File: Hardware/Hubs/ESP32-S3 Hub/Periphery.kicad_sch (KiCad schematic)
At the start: 13 parts, among them SW1 Mitsumi R-667996, SW2 Mitsumi R-667996, SW3 DS04-254-2-04BK-SMT, U2 74HC595, U3 THVD1420DRLR

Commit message: Started Proto 2 again
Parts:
- removed R21, R22, R23: 120 ohm, Resistor_SMD:R_0402_1005Metric, symbol Device:R_Small
- removed SW3: DS04-254-2-04BK-SMT, Button_Switch_SMD:SW_DIP_SPSTx04_Slide_Omron_A6S-410x_W8.9mm_P2.54mm, symbol Switch:SW_DIP_x04
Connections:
- no-connect marks 4 -> 2

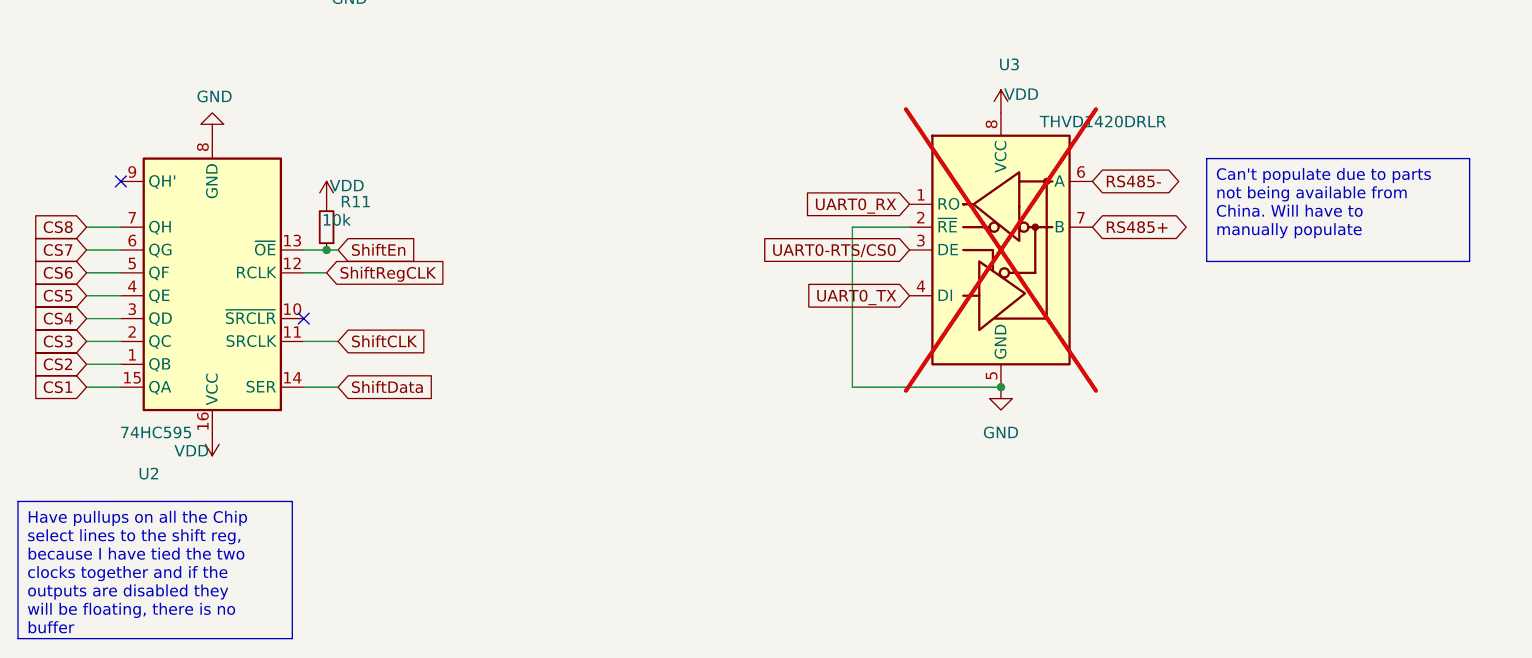
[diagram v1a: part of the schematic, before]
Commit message: Updated connectors in schem and pcb
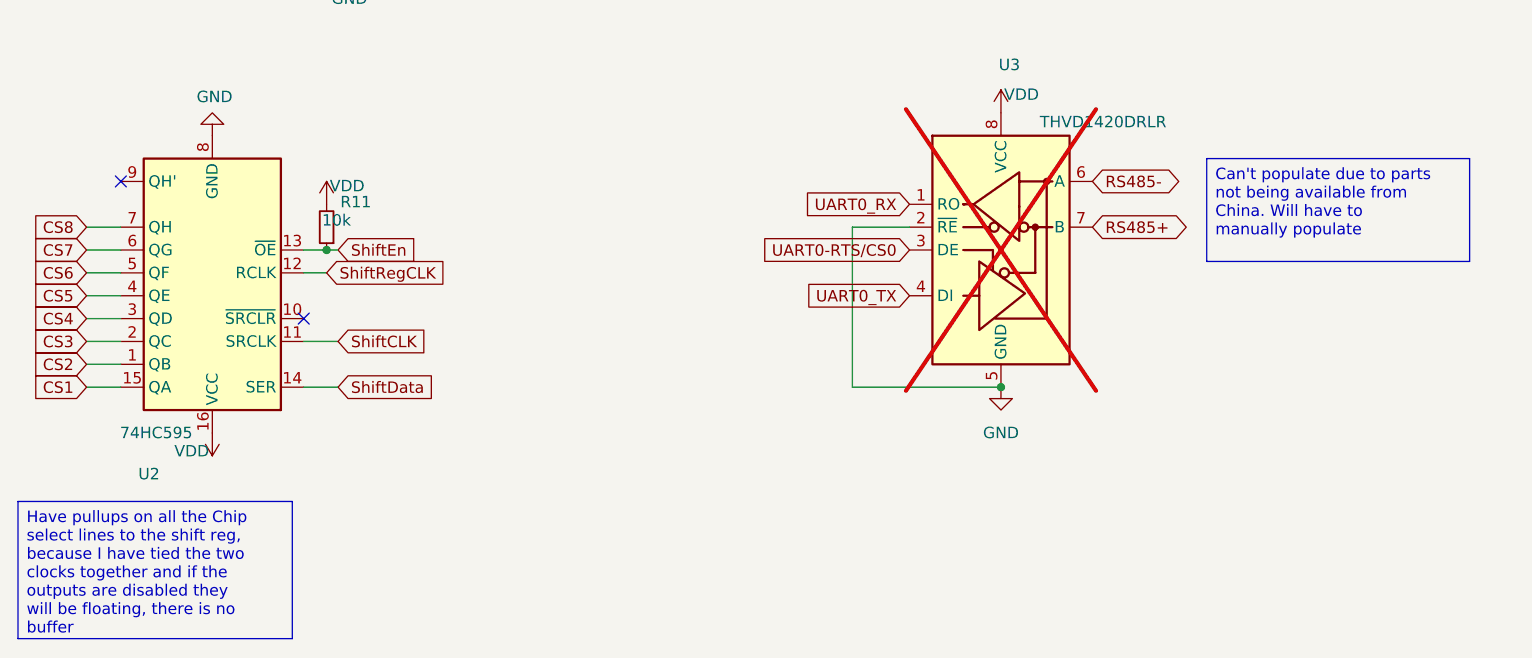
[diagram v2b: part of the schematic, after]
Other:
- title: CACKLE -  Hub/Periphery -> CACKLE -  Hub

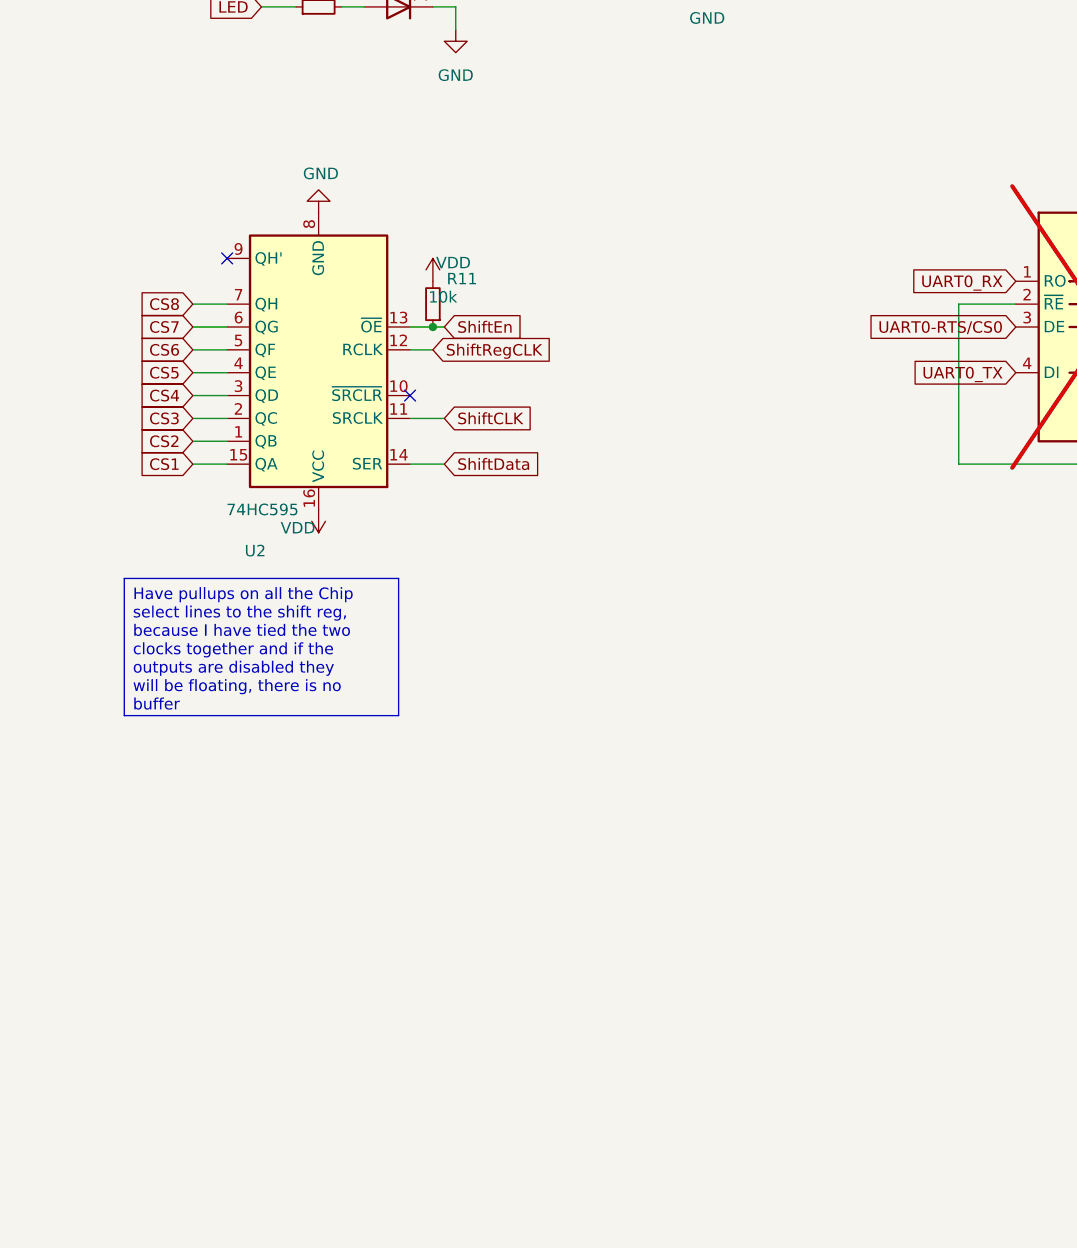
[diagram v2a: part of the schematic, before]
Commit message: Changed peripheral, tied PWM to shift reg, program pins
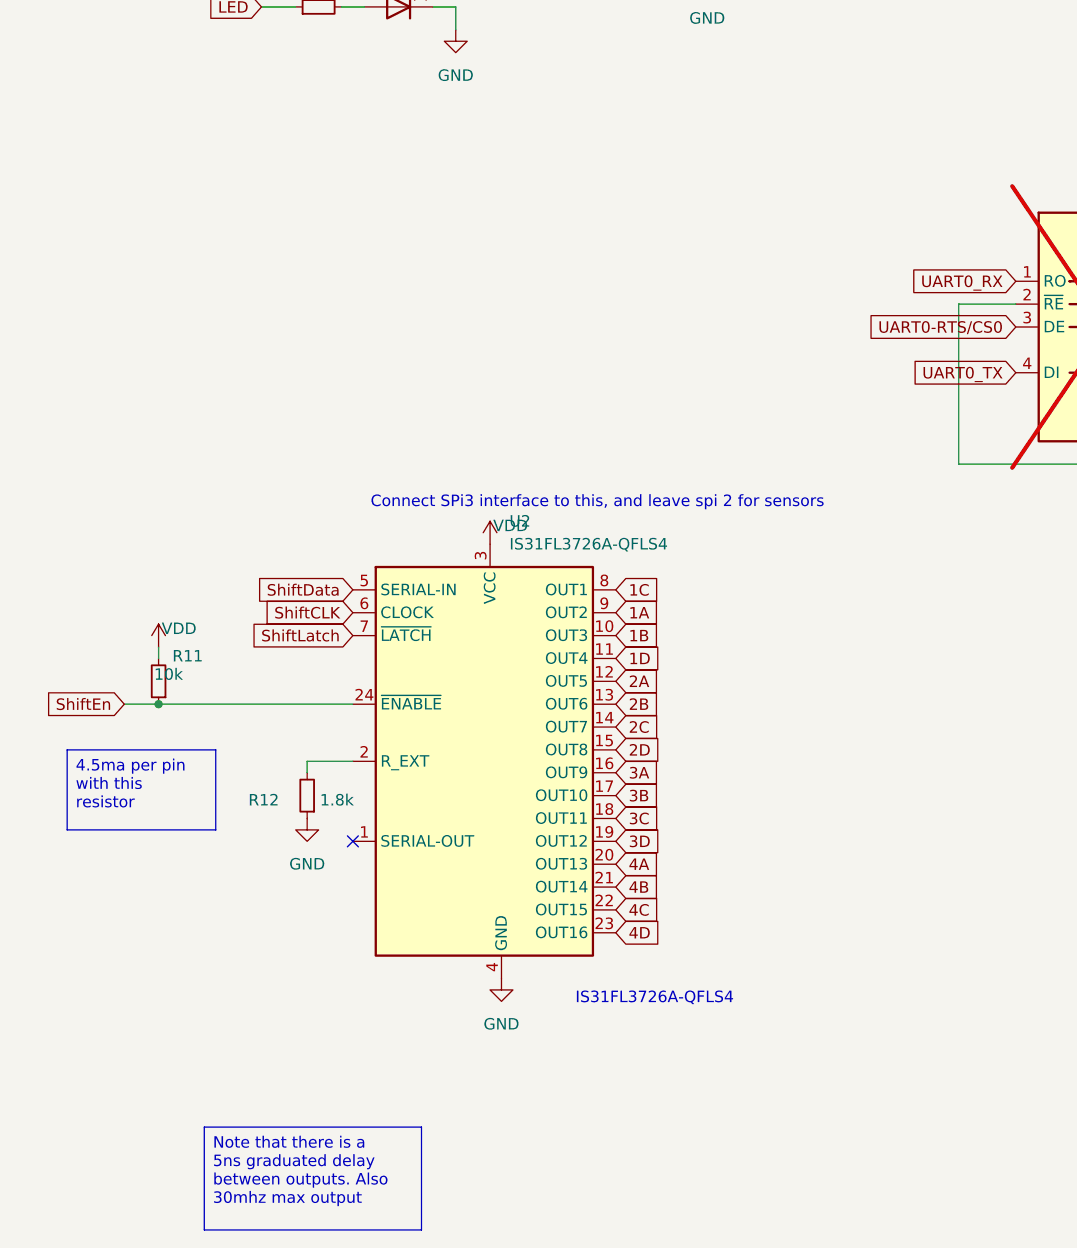
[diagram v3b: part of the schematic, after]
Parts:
- removed U2: 74HC595, Package_DFN_QFN:DHVQFN-16-1EP_2.5x3.5mm_P0.5mm_EP1x2mm, symbol 74xx:74HC595
- added R12: 1.8k, Resistor_SMD:R_0402_1005Metric, symbol Device:R_Small
- added U2: IS31FL3726A-QFLS4, Package_DFN_QFN:QFN-24-1EP_4x4mm_P0.5mm_EP2.7x2.7mm, symbol custom_Driver_LED:IS31FL3726A
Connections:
- net GND: now also R12.1, U2.25 (GND), U2.4 (GND)
- net ShiftCLK: now also U2.6 (CLOCK)
- net ShiftData: now also U2.5 (SERIAL-IN)
- net ShiftEn: now also U2.24 (~{ENABLE})
- net VDD: now also U2.3 (VCC)
- new net: R12.2, U2.2 (R_EXT)
- new net 1A: U2.9 (OUT2)
- new net 1B: U2.10 (OUT3)
- new net 1C: U2.8 (OUT1)
- new net 1D: U2.11 (OUT4)
- new net 2A: U2.12 (OUT5)
- new net 2B: U2.13 (OUT6)
- new net 2C: U2.14 (OUT7)
- new net 2D: U2.15 (OUT8)
- new net 3A: U2.16 (OUT9)
- new net 3B: U2.17 (OUT10)
- new net 3C: U2.18 (OUT11)
- new net 3D: U2.19 (OUT12)
- new net 4A: U2.20 (OUT13)
- new net 4B: U2.21 (OUT14)
- new net 4C: U2.22 (OUT15)
- new net 4D: U2.23 (OUT16)
- new net ShiftLatch: U2.7 (~{LATCH})
- no-connect marks 2 -> 1
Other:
- note added: "Connect SPi3 interface to this, and leave spi 2 for sensors"
- note added: "IS31FL3726A-QFLS4"
- moved on the sheet: R11

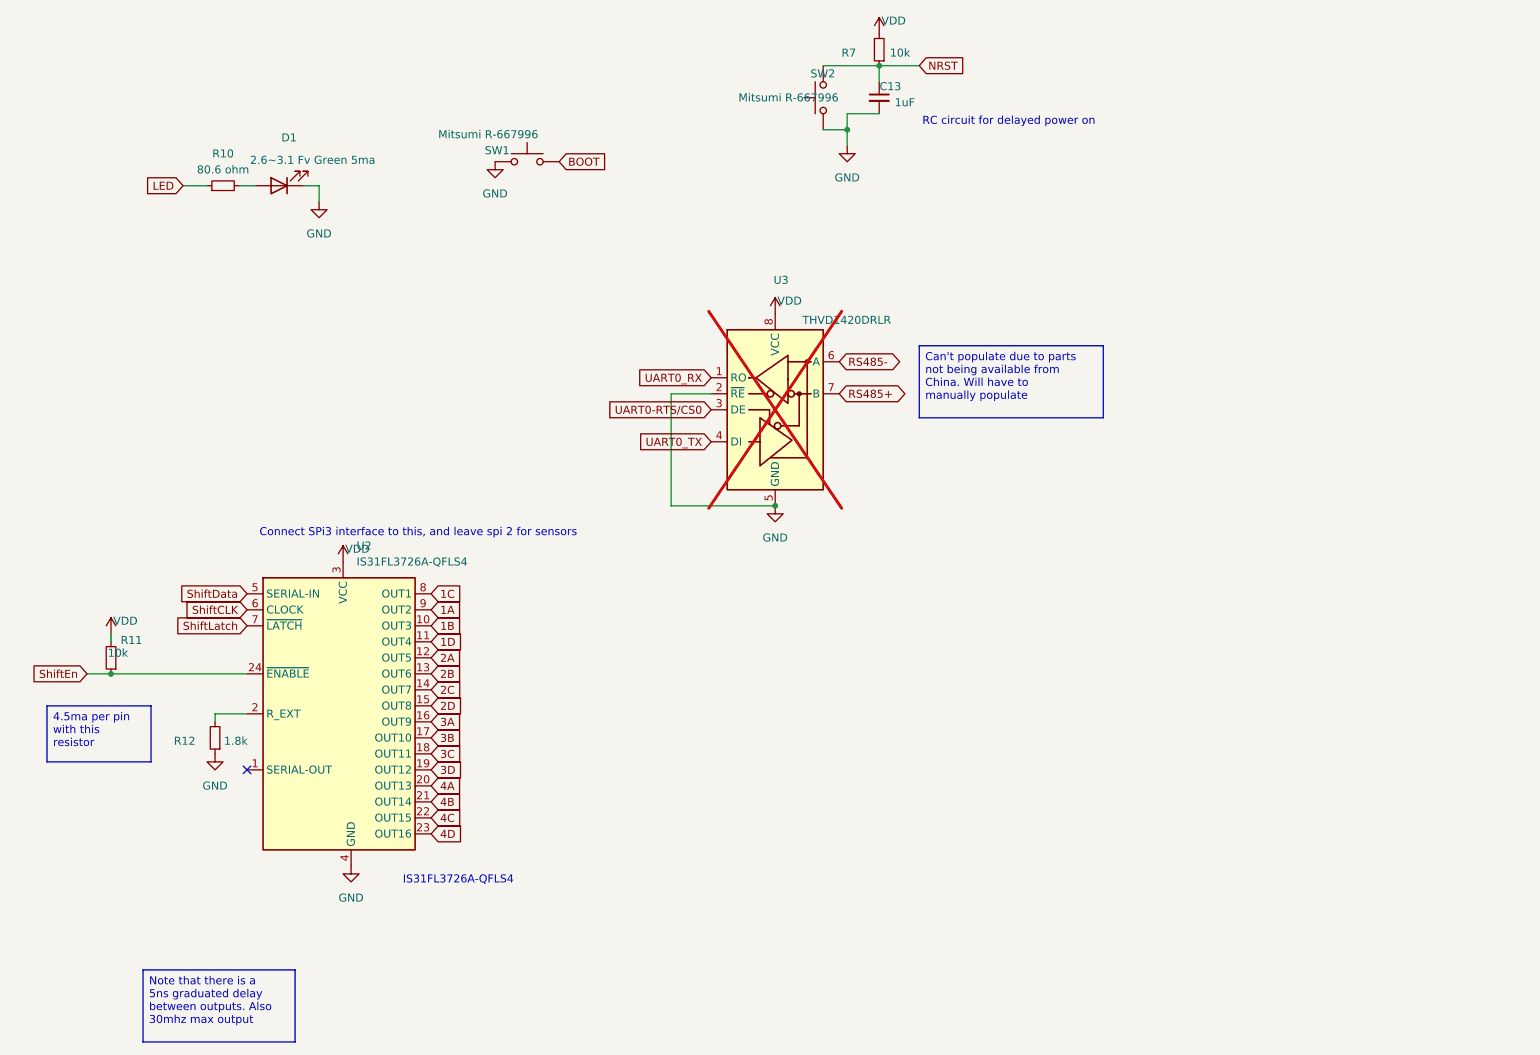
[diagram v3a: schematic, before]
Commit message: Added future design expansion comments, re arrange components to fit better
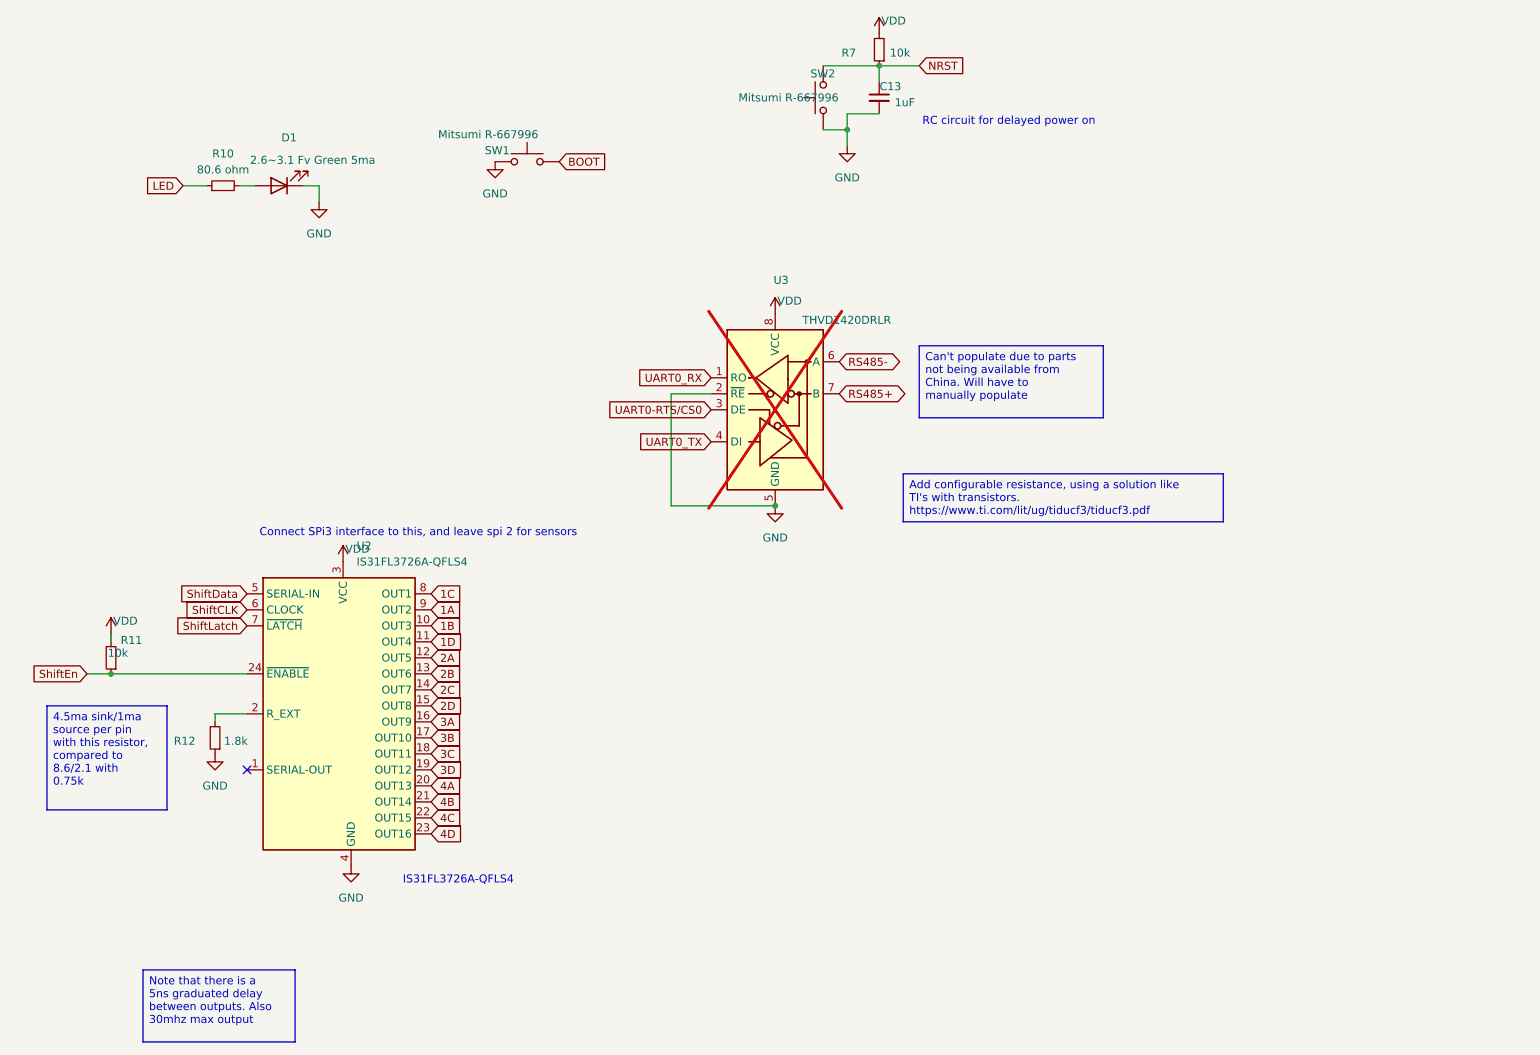
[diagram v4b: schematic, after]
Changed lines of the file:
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@@
+		)
+	)
+	(text_box "Add configurable resistance, using a solution like TI's with transistors. https://www.ti.com/lit/ug/tiducf3/tiducf3.pdf"
+		(exclude_from_sim no)
+		(at 165.1 96.52 0)
+		(size 50.8 7.62)
+		(margins 0.9525 0.9525 0.9525 0.9525)
+		(stroke
+			(width 0)
+			(type solid)
+		)
+		(fill
+			(type none)
+		)
+		(effects
+			(font
+				(size 1.27 1.27)
+			)
+			(justify left top)
+			(href "https://www.ti.com/lit/ug/tiducf3/tiducf3.pdf")
 		)
 	)
@@
 		)
 	)
-	(text_box "4.5ma per pin with this resistor"
+	(text_box "4.5ma sink/1ma source per pin with this resistor, compared to 8.6/2.1 with 0.75k"
 		(exclude_from_sim no)
 		(at 29.21 133.35 0)
-		(size 16.51 8.89)
+		(size 19.05 16.51)
 		(margins 0.9525 0.9525 0.9525 0.9525)
 		(stroke
